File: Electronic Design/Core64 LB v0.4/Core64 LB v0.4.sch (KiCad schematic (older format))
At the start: 15 parts, among them J4 TSM-106-03-T-DV‎, U2 Teensy-LC, U3 M24C01-RMN, U4 SN74LV1T125DBVR

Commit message: Correct Logic Board filenames to LB from CB
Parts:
- removed JP2: SolderJumper_3_Bridged123, Jumper:SolderJumper-3_P1.3mm_Bridged123_Pad1.0x1.5mm_NumberLabels, symbol Jumper:SolderJumper_3_Bridged123
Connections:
- wire segments 78 -> 80
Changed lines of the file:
@@
 EESchema Schematic File Version 4
-LIBS:Core64 CB v0.4-cache
+LIBS:Core64 LB v0.4-cache
 EELAYER 29 0
 EELAYER END
@@
 U 5E755AC8
 F0 "Core Array Driver" 50
-F1 "Core64 CB v0.4 Driver.sch" 50
+F1 "Core64 LB v0.4 Driver.sch" 50
 $EndSheet
 Text Notes 2650 750  0    118  ~ 0
@@
 U 5E75D6AB
 F0 "SENSE" 50
-F1 "Core64 CB v0.4 Sense.sch" 50
+F1 "Core64 LB v0.4 Sense.sch" 50
 $EndSheet
 $Sheet
@@
 U 5EA63449
 F0 "IO Expansion" 50
-F1 "Core64 CB v0.4 Expansion.sch" 50
+F1 "Core64 LB v0.4 Expansion.sch" 50
 $EndSheet
 $Comp
@@
 U 5E7548ED
 F0 "Power" 50
-F1 "Core64 CB v0.4 Power.sch" 50
+F1 "Core64 LB v0.4 Power.sch" 50
 $EndSheet
 Text GLabel 1900 2500 0    50   BiDi ~ 0
@@
 Wire Wire Line
 	7650 5800 7650 6100
-$Comp
-L Jumper:SolderJumper_3_Bridged123 JP?
-U 1 1 5EA7ABDA
-P 7450 5800
-AR Path="/5EA63449/5EA7ABDA" Ref="JP?"  Part="1"
-AR Path="/5EA7ABDA" Ref="JP2"  Part="1"
-F 0 "JP2" H 7450 5915 50  0000 C CNN
-F 1 "SolderJumper_3_Bridged123" H 8050 5750 50  0000 C CNN
-F 2 "Jumper:SolderJumper-3_P1.3mm_Bridged123_Pad1.0x1.5mm_NumberLabels" H 7450 5800 50  0001 C CNN
-F 3 "~" H 7450 5800 50  0001 C CNN
-	1    7450 5800
-	-1   0    0    1
-$EndComp
 Wire Wire Line
 	7150 6400 7650 6400
@@
 	7250 5800 7250 5900
 Wire Wire Line
-	7450 5600 7450 5650
+	7450 5600 7450 5800
 Wire Wire Line
 	4200 4200 4250 4200
@@
 Text GLabel 1150 2400 0    50   Input ~ 0
 TEENSY_GND
+Wire Wire Line
+	7250 5800 7450 5800
+Connection ~ 7450 5800
+Wire Wire Line
+	7450 5800 7650 5800
 $EndSCHEMATC

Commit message: Swap in Teensy 3.2 from LC, set schematic sheet sizes to A, update power schematic
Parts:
- removed JP1: SolderJumper_3_Bridged12, Jumper:SolderJumper-3_P1.3mm_Bridged12_Pad1.0x1.5mm_NumberLabels, symbol Jumper:SolderJumper_3_Bridged12
- removed U2: Teensy-LC, Teensy:Teensy30_31_32_LC_SMD_SOCKETS, symbol Teensy:Teensy-LC
- added U2: Teensy3.2, symbol Teensy:Teensy3.2
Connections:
- net labels added: V_MON
- net labels removed: IOEXP_ID32_INT_A, IOEXP_ID32_INT_B, IOEXP_ID33_INT_A, IOEXP_ID33_INT_B, SAO3_GPIO1, SAO3_GPIO2, TEENSY_GND, VSW_HALF_VOL_MONITOR
- wire segments 80 -> 59
- no-connect marks 23 -> 11
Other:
- note added: "*** CUT THE USB-VIN bridge on TEENSY 3.2 ***"
- note added: "I2C ADDRESS TABLE\nRequired\n AMBIENT LIGHT SENSOR: 0X29 (47 decimal)\n HALL SENSOR 1: 0x30 (48 decimal)\n HALL SENSOR 2: 0x31 (49 decimal)\n HALL SENSOR 3: 0x32 (50 decimal)\n HALL SENSOR 4: 0x33 (51 decimal)\n EEPROM: 0b1010111, 0x57 (87 decimal)\nOptional\n OLED: 0x3C (60 decimal)\n AND!XOR GPIO Expander MCP23017 0x20 (32 decimal)\n AND!XOR EEPROM AT24C32r 0x50 (80 decimal)\n\nAll 7-bit addres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"
- note added: "Reads 1/4 voltage of +VSW\n(after RPP)"
- note added: "TEENSY 3.2 MCU CONNECTIONS"
- note added: "Teensy LC has incoming USB power/programming on board."
- note added: "VIN must be supplied TO the Teensy\nbecause VIN-VUSB is cut. The \nLogic Board provides it here."
- note removed: "I2C ADDRESS TABLE\nRequired\n IO EXPANDER 1: 0x26 (38 decimal)\n IO EXPANDER 2: 0x27 (39 decimal)\n HALL SENSOR 1: 0x30 (48 decimal)\n HALL SENSOR 2: 0x31 (49 decimal)\n HALL SENSOR 3: 0x32 (50 decimal)\n HALL SENSOR 4: 0x33 (51 decimal)\n EEPROM: 0b1010111, 0x57 (87 decimal)\nOptional\n OLED: 0x3C (60 decimal)\n AND!XOR GPIO Expander MCP23017 0x20 (32 decimal)\n AND!XOR EEPROM AT24C32r 0x50 (80 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"
- note removed: "Reads 1/2 +VSW (battery) voltage"
- note removed: "TEENSY MCU CONNECTIONS"
- note removed: "Teensy LC has incoming USB power/programming on board.\n*** CUT THE USB-VIN bridge. ***"
- note removed: "Try not to use any of these\nto avoid the need to populate\nthis end row header on the PCB."

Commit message: Add regulator and battery connector data sheets, footprints, symbols
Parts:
- removed L4: Core_64_Github_Link, Core_Memory_8x8_Array:Github_Link_Small, symbol CORE_64_LIBRARY:Core_64_Github_Link
- added C1: 1000uF, Capacitor_SMD:CP_Elec_10x10, symbol Device:CP1_Small
- C4, C5: symbol Device:CP1_Small -> Device:C
- U2: footprint (none) -> Teensy:Teensy30_31_32_LC_SMD_SOCKETS
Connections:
- net labels added: 5V0, LED_MATRIX_5V0_SIG
- net labels removed: +VSW, LED_MATRIX_+VSW_SIG, TEENSY_VIN
- wire segments 59 -> 62
- no-connect marks 11 -> 9
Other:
- note added: "All non-polarized capacitors are ceramic unless otherwise noted."
- note added: "LED ARRAY DRIVE AND LEVEL SHIFT"
- note added: "PLACE\nCAPACITOR\nNEAR\nLED MATRIX"
- note removed: "LED ARRAY (PARTIAL RASPI HEADER)"
- note removed: "LED ARRAY DRIVE LEVEL SHIFT"
- moved on the sheet: J4, R5, U4

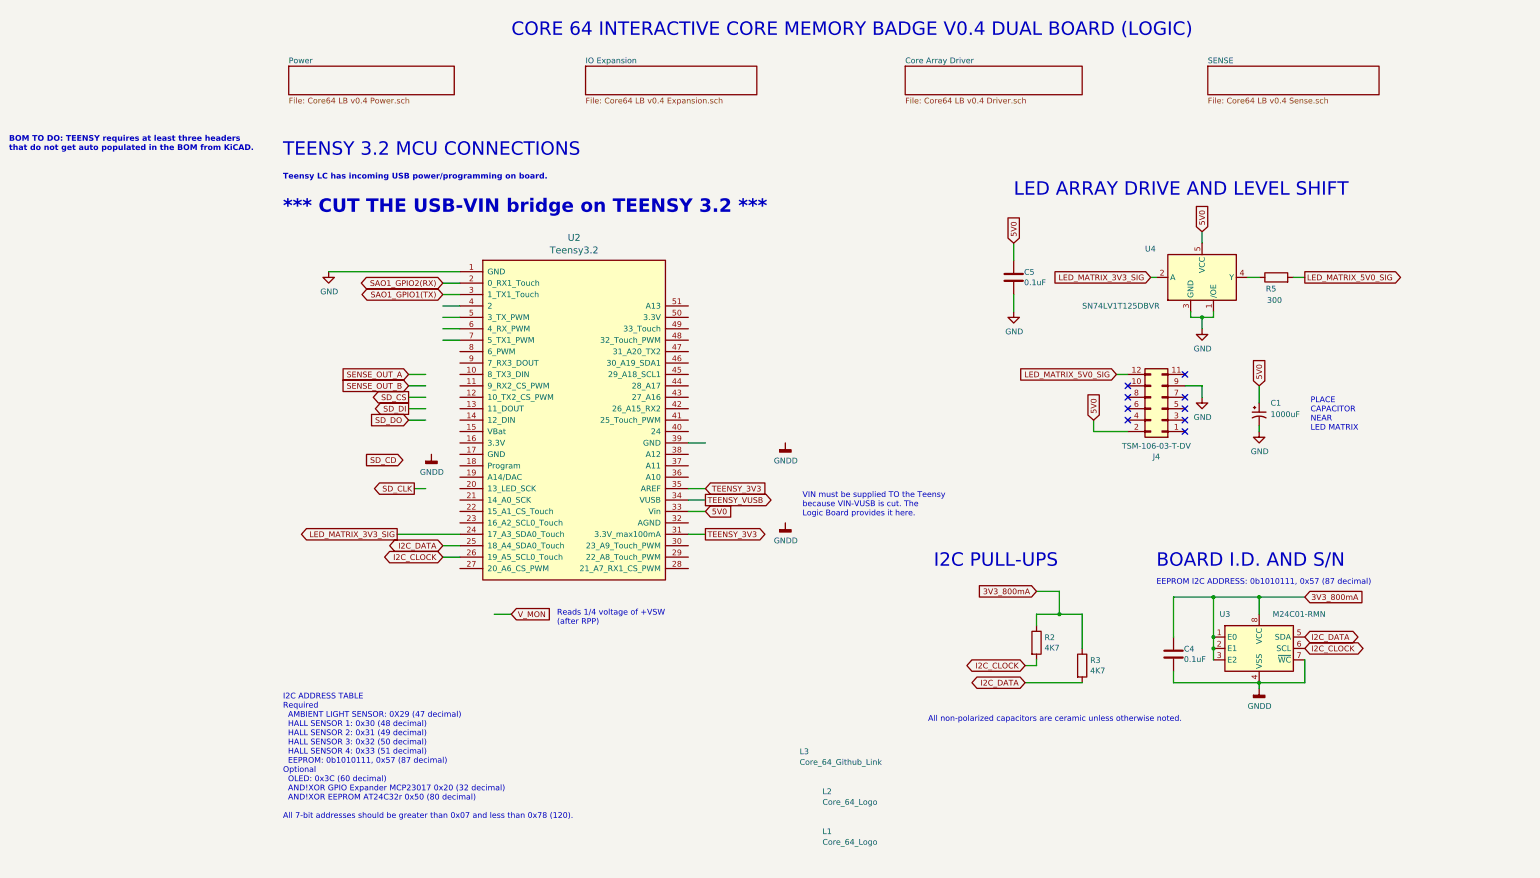
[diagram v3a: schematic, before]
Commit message: Complete LB power schematic, add 3-to-8 decoder
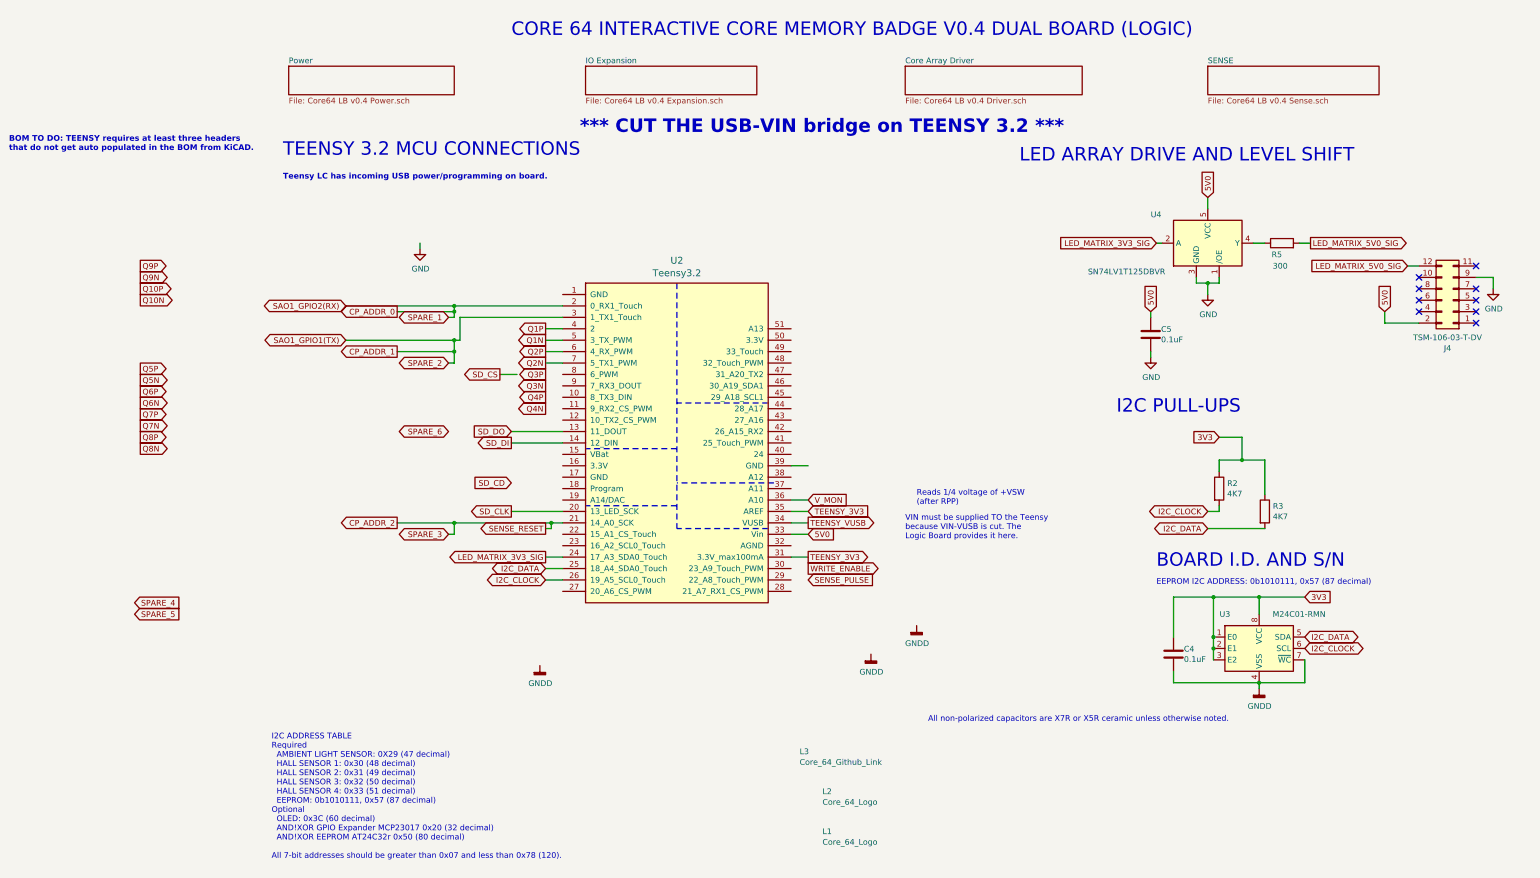
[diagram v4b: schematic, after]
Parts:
- removed C1: 1000uF, Capacitor_SMD:CP_Elec_10x10, symbol Device:CP1_Small
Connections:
- net labels added: 3V3, CP_ADDR_0, CP_ADDR_1, CP_ADDR_2, Q10N, Q10P, Q1N, Q1P, Q2N, Q2P, Q3N, Q3P, Q4N, Q4P, Q5N, Q5P, Q6N, Q6P, Q7N, Q7P, Q8N, Q8P, Q9N, Q9P, SENSE_PULSE, SENSE_RESET, SPARE_1, SPARE_2, SPARE_3, SPARE_4, SPARE_5, SPARE_6, WRITE_ENABLE
- net labels removed: 3V3_800mA, SENSE_OUT_A, SENSE_OUT_B
- wire segments 62 -> 77
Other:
- note added: "All non-polarized capacitors are X7R or X5R ceramic unless otherwise noted."
- note removed: "All non-polarized capacitors are ceramic unless otherwise noted."
- note removed: "PLACE\nCAPACITOR\nNEAR\nLED MATRIX"
- moved on the sheet: C5, J4, R2, R3, R5, U2, U4

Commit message: Add 3-to-8 and begin other expansion on schematic
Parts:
- R5: value 300 -> 470
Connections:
- net labels added: SAO_GPIO1, SAO_GPIO2, SP1_SAO1_CPA0, SPI_SDI, SPI_SDO
- net labels removed: SAO1_GPIO1(TX), SAO1_GPIO2(RX), SD_DI, SD_DO
- wire segments 77 -> 74
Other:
- note added: "Silkscreen: 5V0 ONLY"
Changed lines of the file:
@@
 Text Notes 6200 4850 0    50   ~ 0
 Reads 1/4 voltage of +VSW\n(after RPP)
-Text Notes 650  2000 0    50   ~ 10
+Text Notes 600  2150 0    50   ~ 10
 Teensy LC has incoming USB power/programming on board.
 Wire Wire Line
@@
 	3100 5500 2950 5500
 Wire Wire Line
-	1200 3100 2150 3100
+	1150 3100 2150 3100
 Wire Wire Line
 	2950 3400 3100 3400
@@
 AR Path="/5EA33CBB" Ref="R5"  Part="1"
 F 0 "R5" V 9300 2550 50  0000 L CNN
-F 1 "300" V 9200 2500 50  0000 L CNN
+F 1 "470" V 9200 2500 50  0000 L CNN
 F 2 "Resistor_SMD:R_0805_2012Metric" V 9330 2550 50  0001 C CNN
 F 3 "~" H 9400 2550 50  0001 C CNN
@@
 F1 "Core64 LB v0.4 Power.sch" 50
 $EndSheet
-Text GLabel 1200 3100 0    50   BiDi ~ 0
-SAO1_GPIO2(RX)
 Wire Wire Line
 	1850 2550 1850 2600
-Text GLabel 1200 3400 0    50   BiDi ~ 0
-SAO1_GPIO1(TX)
+Text GLabel 1150 3100 0    50   BiDi ~ 0
+SAO_GPIO1
 $Comp
 L Logic_LevelTranslator:SN74LV1T125DBVR U4
@@
 	8850 2900 8750 2900
 Connection ~ 8750 2900
-Text Notes 7100 1850 0    118  ~ 0
+Text Notes 7100 1950 0    118  ~ 0
 LED ARRAY DRIVE AND LEVEL SHIFT
-Text Notes 650  1800 0    118  ~ 0
+Text Notes 600  1950 0    118  ~ 0
 TEENSY 3.2 MCU CONNECTIONS
 Text Notes 550  7950 0    50   ~ 0
@@
 Text GLabel 2550 3700 0    50   Output ~ 0
 SD_CS
-Text GLabel 2650 4300 0    50   Output ~ 0
-SD_DI
-Text GLabel 2650 4200 0    50   Input ~ 0
-SD_DO
+Text GLabel 2650 4300 0    50   Input ~ 0
+SPI_SDI
 Text GLabel 2650 4900 0    50   Output ~ 0
 SD_CLK
@@
 Wire Wire Line
 	3100 5300 2950 5300
-Text Notes 3250 1600 0    118  ~ 24
+Text Notes 1100 1700 0    236  ~ 47
 *** CUT THE USB-VIN bridge on TEENSY 3.2 ***
 Text Notes 6100 5150 0    50   ~ 0
@@
 Text GLabel -600 2850 2    50   Output ~ 0
 Q9N
-Text GLabel 2950 5050 0    50   Output ~ 0
+Text GLabel 1150 4650 0    50   Output ~ 0
 SENSE_RESET
 Text GLabel 5250 5400 2    50   Output ~ 0
@@
 	2150 3100 3100 3100
 Wire Wire Line
-	1200 3400 2150 3400
+	1150 3400 2150 3400
 Wire Wire Line
 	2200 3400 2200 3200
@@
 	4900 3950 4100 3950
 Wire Wire Line
-	3100 5000 3000 5000
-Wire Wire Line
 	2100 5100 2150 5100
 Wire Wire Line
@@
 Wire Wire Line
 	2150 5000 1650 5000
-Text GLabel 2100 4200 0    50   BiDi ~ 0
+Text GLabel 2100 4100 0    50   BiDi ~ 0
 SPARE_6
-Wire Wire Line
-	2950 5050 3000 5050
-Wire Wire Line
-	3000 5050 3000 5000
-Connection ~ 3000 5000
-Wire Wire Line
-	3000 5000 2150 5000
+Text Notes 10400 3650 0    50   ~ 0
+Silkscreen: 5V0 ONLY
+Text GLabel 1150 3400 0    50   BiDi ~ 0
+SAO_GPIO2
+Wire Wire Line
+	2150 5000 3100 5000
+Text GLabel 2650 4200 0    50   Output ~ 0
+SPI_SDO
+Text GLabel 5250 3400 2    50   Output ~ 0
+TEENSY_3V3
+Text GLabel 1350 2900 0    50   BiDi ~ 0
+SP1_SAO1_CPA0
 $EndSCHEMATC

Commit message: Update schematic and XLS pin usage
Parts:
- J4: footprint Connector_PinHeader_2.54mm:PinHeader_2x06_P2.54mm_Vertical_SMD_and_TH -> Connector_PinHeader_2.54mm:PinHeader_2x07_P2.54mm_Vertical_SMD_and_TH; symbol Connector_Generic:Conn_02x06_Odd_Even -> Connector_Generic:Conn_02x07_Odd_Even
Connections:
- net labels added: IR_MOD, LED_ARRAY_3V3_SIG, LED_ARRAY_5V0_SIG, OLED_SPI_CS, OLED_SPI_DC, SAO_G1_or_SPARE_1_or_CP_ADDR_0, SAO_G2_or_SPARE_2_or_CP_ADDR_1, SD_SPI_CD, SD_SPI_CS, SPARE_3_or_CP_ADDR_2, SPARE_ADC_DAC, SPARE_ANA_6, SPARE_ANA_7, SPARE_SPI_CS, SPARE_SPI_DC, SPI_CLK, TEENSYVIEW_SPI_CS, TEENSYVIEW_SPI_DC, TFT_BACKLIGHT, TFT_SPI_CS, TFT_SPI_DC, TFT_SPI_RESET, TOUCH_SPI_CS, VBAT_MON
- net labels removed: CP_ADDR_0, CP_ADDR_1, CP_ADDR_2, LED_MATRIX_3V3_SIG, LED_MATRIX_5V0_SIG, SAO_GPIO1, SAO_GPIO2, SD_CD, SD_CLK, SD_CS, SP1_SAO1_CPA0, SPARE_1, SPARE_2, SPARE_3, SPARE_6, TEENSY_3V3, V_MON
- wire segments 74 -> 122
- no-connect marks 9 -> 13
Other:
- note added: "0X29 (47)\n0x30 (48)\n0x31 (49)\n0x32 (50)\n0x33 (51)\n0x57 (87)"
- note added: "0x3C (60)\n0x20 (32)\n0x50 (80)"
- note added: "3.2” TFT (LED replacement)"
- note added: "8 Core Plane Selector"
- note added: "AMBIENT LIGHT SENSOR\nHALL SENSOR 1\nHALL SENSOR 2\nHALL SENSOR 3\nHALL SENSOR 4\nEEPROM (BOARD ID)"
- note added: "All 7-bit addresses should be greater\nthan 0x07 and less than 0x78 (120)."
- note added: "BOARD ID AND S/N"
- note added: "CORE 64 INTERACTIVE CORE MEMORY BADGE V0.4 LOGIC BOARD"
- note added: "EEPROM I2C ADDRESS: 0b1010111, 0x57 (87)"
- note added: "I2C ADDRESS TABLE"
- note added: "INCLUDED:"
- note added: "OLED\nAND!XOR IO Exp. MCP23017\nAND!XOR EEPROM AT24C32r"
- note added: "OPTIONAL:"
- note added: "Primary Use\n1 Core Plane"
- note added: "QxP is normally high, goes low to activate matrix transistor.\nQxN is normally low, goes high to activate matrix transistor."
- note added: "Reads 1/4 voltage of +VSW\n(after RPP) before regulators."
- note added: "SAO#1/2 GPIO1&2 shared\nwith Core Plane Addressing"
- note added: "SILKSCREEN GRAPHICS"
- note added: "SILKSCREEN MISC."
- note added: "SILKSCREEN UNDER TEENSY: CUT VIN-BUSB"
- note added: "SILKSCREEN: \n5V0 ONLY\nLED ARRAY"
- note added: "TSM-106 (2x6) required\nTSM-107 (2x7) alternate"
- note added: "Teensy 3V3 is only used for AREF.\nCurrent is limited, do not use for\nanything else."
- note added: "VIN (5V) must be supplied TO the Teensy\nbecause VIN-VUSB is cut. The \nLogic Board provides it here."
- note added: "VUSB provides power to main\nLogic Board power switch."
- note removed: "BOARD I.D. AND S/N"
- note removed: "CORE 64 INTERACTIVE CORE MEMORY BADGE V0.4 DUAL BOARD (LOGIC)"
- note removed: "EEPROM I2C ADDRESS: 0b1010111, 0x57 (87 decimal)"
- note removed: "I2C ADDRESS TABLE\nRequired\n AMBIENT LIGHT SENSOR: 0X29 (47 decimal)\n HALL SENSOR 1: 0x30 (48 decimal)\n HALL SENSOR 2: 0x31 (49 decimal)\n HALL SENSOR 3: 0x32 (50 decimal)\n HALL SENSOR 4: 0x33 (51 decimal)\n EEPROM: 0b1010111, 0x57 (87 decimal)\nOptional\n OLED: 0x3C (60 decimal)\n AND!XOR GPIO Expander MCP23017 0x20 (32 decimal)\n AND!XOR EEPROM AT24C32r 0x50 (80 decimal)\n\nAll 7-bit addres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"
- note removed: "Reads 1/4 voltage of +VSW\n(after RPP)"
- note removed: "Silkscreen: 5V0 ONLY"
- note removed: "VIN must be supplied TO the Teensy\nbecause VIN-VUSB is cut. The \nLogic Board provides it here."
- moved on the sheet: C4, C5, R2, R3, R5, U2, U3, U4
